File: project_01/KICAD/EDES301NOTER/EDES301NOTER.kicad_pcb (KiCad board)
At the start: 2 copper layers, 61 parts, among them J1 FH12-24S-0.5SH55, Q1 S8050, Q2 BSS84, Q3 BSS84, Q4 BSS84, Q5 BSS138, Q6 BSS84, Q7 BSS138, U1 POCKETBEAGLE, U2 DRV5032FCDBZR, U3 TPS613222ADBVR, U7 PMF250XNEX

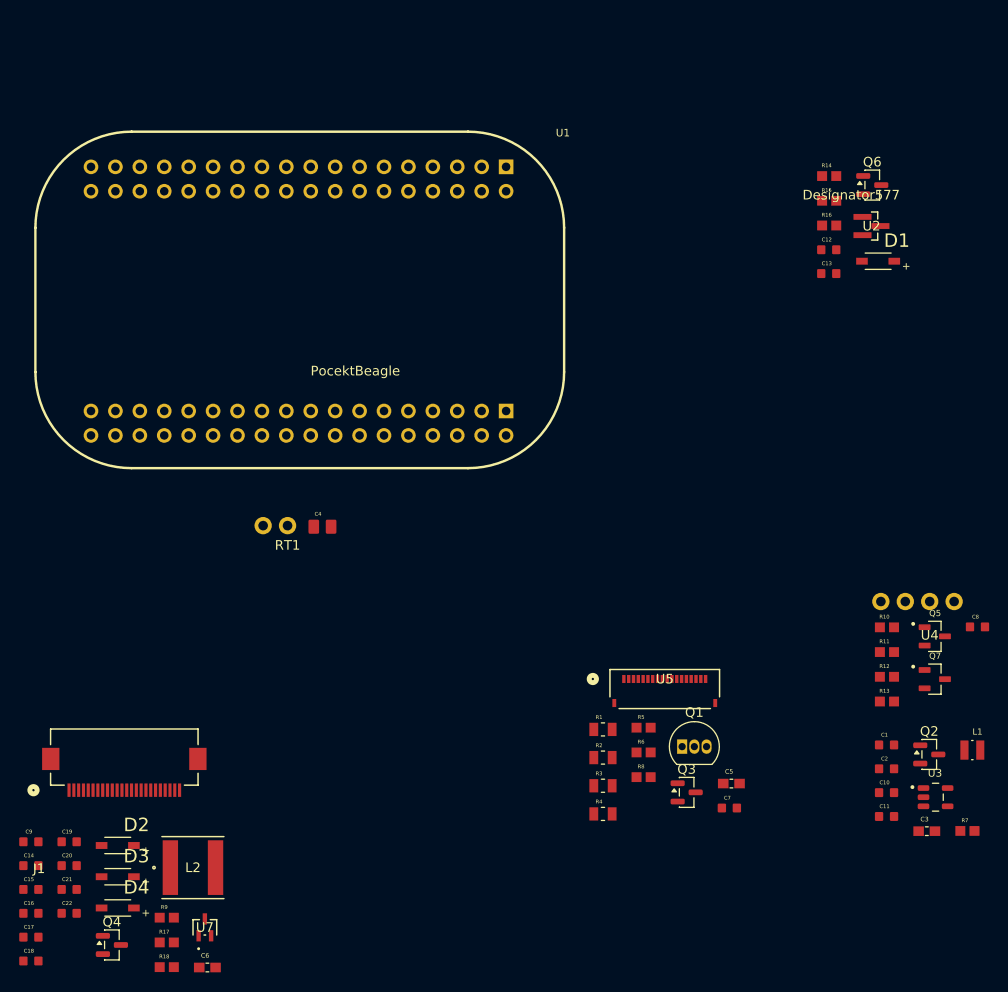
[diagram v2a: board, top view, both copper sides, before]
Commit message: Revise Boost5V schematic and add STIKE symbols
Refactor Boost5V.kicad_sch: updated title block and paper size, reorganized and renamed many symbol definitions (capacitor/inductor/diode/resistor/LED/driver), adjusted pin assignments, footprints, datasheet links and symbol graphics. Added new STIKE-related schematic symbols (Slide Switch, LipoConnection) and multiple KiCad footprint/symbol files under KICAD Files. Added project backup zips and freerouting.dsn, removed a temporary .kicad_sch.lck, and updated project metadata files (.kicad_pcb, .kicad_prl, .kicad_pro, .kicad_sch).
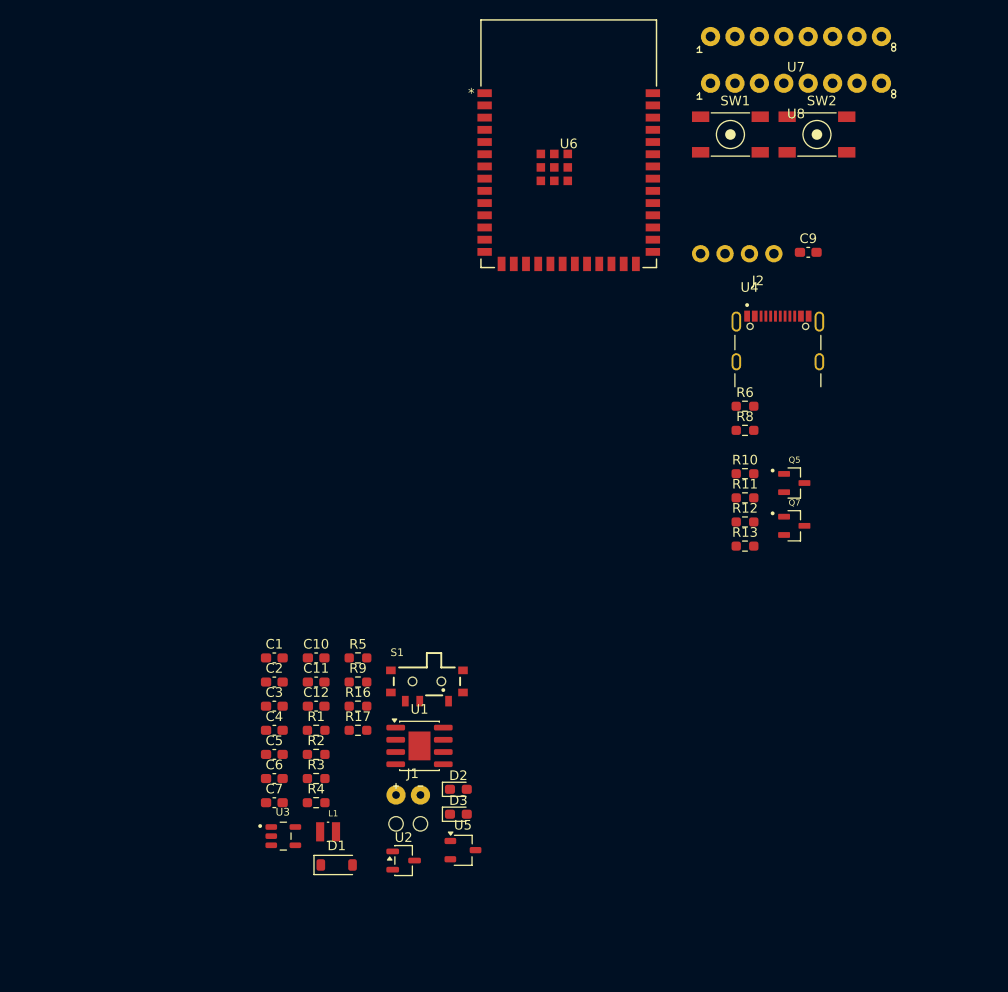
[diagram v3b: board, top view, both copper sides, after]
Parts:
- removed C13, C14, C16, C17, C19, C20, C21, C22, C8: 1uF, Footprints:CAPC1608X90N
- removed C15, C18: 4.7uF, Footprints:CAPC1608X90N
- removed D4: B0530W-7-F, B0530W-7-F:SOD3715X145N
- removed L2: 47uH, IFSC2020DEER470M01:IND_IFSC-2020DE-01_VIS
- removed Q1: S8050, Package_TO_SOT_THT:TO-92_Inline
- removed Q2, Q3, Q4, Q6: BSS84, Package_TO_SOT_SMD:SOT-23
- removed R14: 10k, Footprints:RESC1607X60N
- removed R15, R7: 100k, Footprints:RESC1607X60N
- removed R18: 2.2, Footprints:RESC1607X60N
- removed RT1: NXRT15XH103FA1B040, HomeBrew:2_Wire_Connector
- added J2: UJ20-C-H-G-SMT-1-P16-TR, STIKE:SAMESKY_UJ20-C-H-G-SMT-1-P16-TR, F.Cu at (141.7, 72.0)
- added S1: ~, STIKE:450404015514, F.Cu at (105.2, 102.7)
- added SW1: Boot, STIKE:MembraneButton, F.Cu at (136.8, 56.0)
- added SW2: RST, STIKE:MembraneButton, F.Cu at (145.8, 56.0)
- added U6: ESP32-S3-WROOM-1-N16R8, STIKE:ESP32-S3-WROOM-1_EXP, F.Cu at (120.0, 46.8)
- added U8: ~, STIKE:THROUGH8, F.Cu at (142.3, 40.5)
- C1, C10, C11, C12, C2, C9: footprint Footprints:CAPC1608X90N -> Capacitor_SMD:C_0603_1608Metric_Pad1.08x0.95mm_HandSolder
- C3, C6: value 0.1uF -> 1uF; footprint Footprints:CAPC1608X90 -> Capacitor_SMD:C_0603_1608Metric_Pad1.08x0.95mm_HandSolder
- C4: value 47uF -> 1uF; footprint Footprints:CAPC2012X145N -> Capacitor_SMD:C_0603_1608Metric_Pad1.08x0.95mm_HandSolder
- C5: value 0.1uF -> 4.7uF; footprint Footprints:CAPC1608X90 -> Capacitor_SMD:C_0603_1608Metric_Pad1.08x0.95mm_HandSolder
- C7: value 1uF -> 0.1uF; footprint Footprints:CAPC1608X90N -> Capacitor_SMD:C_0603_1608Metric_Pad1.08x0.95mm_HandSolder
- D1: value B0530W-7-F -> BAT41ZFILM; footprint B0530W-7-F:SOD3715X145N -> Diode_SMD:D_SOD-123
- D2: value B0530W-7-F -> LED_RED; footprint B0530W-7-F:SOD3715X145N -> Diode_SMD:D_0603_1608Metric_Pad1.05x0.95mm_HandSolder
- D3: value B0530W-7-F -> LED_GRN; footprint B0530W-7-F:SOD3715X145N -> Diode_SMD:D_0603_1608Metric_Pad1.05x0.95mm_HandSolder
- J1: value FH12-24S-0.5SH55 -> ~; footprint CF4224FH0R0-05-NH:CONN24X1_FH12-24S-0.5SH55_HIR -> STIKE:LipoConnection
- R1, R2, R3, R4: value 10R -> 1K; footprint Footprints:RESC2012X60N -> Resistor_SMD:R_0603_1608Metric_Pad0.98x0.95mm_HandSolder
- R10, R11, R12, R13, R16, R5: footprint Footprints:RESC1607X60N -> Resistor_SMD:R_0603_1608Metric_Pad0.98x0.95mm_HandSolder
- R17: value 1M -> 1K; footprint Footprints:RESC1607X60N -> Resistor_SMD:R_0603_1608Metric_Pad0.98x0.95mm_HandSolder
- R6: value 1K -> 5.1K; footprint Footprints:RESC1607X60N -> Resistor_SMD:R_0603_1608Metric_Pad0.98x0.95mm_HandSolder
- R8: value 100k -> 5.1K; footprint Footprints:RESC1607X60N -> Resistor_SMD:R_0603_1608Metric_Pad0.98x0.95mm_HandSolder
- R9: value 100k -> 1K; footprint Footprints:RESC1607X60N -> Resistor_SMD:R_0603_1608Metric_Pad0.98x0.95mm_HandSolder
- U1: value POCKETBEAGLE -> TPB4056A20-ES1R; footprint POCKETBEAGLE (1):POCKETBEAGLE -> STIKE:TPB4056A20-ES1R
- U2: value DRV5032FCDBZR -> DRV5032FADBZR; footprint DRV5032FCDBZR:DBZ0003A-IPC_A -> Package_TO_SOT_SMD:SOT-23-3
- U5: value ~ -> XC6206P332MR-G; footprint FH34SRJ-18S-0.5SH:CONN18x1_FH34SRJ-18S-0.5SH50_HIR -> Package_TO_SOT_SMD:TSOT-23
- U7: value PMF250XNEX -> ~; footprint PMF250XNEX:PMF250XNEX_NEX -> STIKE:THROUGH8
- moved U7 110.5 mm to (142.3, 35.6)
- moved C9 101.5 mm to (144.9, 58.0)
- moved D1 84.4 mm to (95.8, 121.8)
- moved U2 82.0 mm to (102.8, 121.3)
- moved C12 71.4 mm to (93.7, 105.3)
- moved R16 70.0 mm to (98.1, 105.3)
- moved C3 69.1 mm to (89.4, 105.3)
- moved U3 68.0 mm to (90.3, 118.8)
- moved L1 67.6 mm to (94.9, 118.3)
- moved U1 65.5 mm to (104.5, 109.4), turned to 0 degrees
- moved C1 64.3 mm to (89.4, 100.2)
- moved C2 64.3 mm to (89.4, 102.8)
- moved C10 61.0 mm to (93.7, 100.2)
- moved C11 61.0 mm to (93.7, 102.8)
- moved C5 47.6 mm to (89.4, 110.3)
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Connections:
- net /CardKB/CARD_SCL renamed /ESP32-S3-N16R8/KEY_SDA
- net /CardKB/CARD_SDA renamed /ESP32-S3-N16R8/KEY_SCL
- C1 pad 1: Net-(Q2-D) -> /Power Circuitry/BAT+
- C1 pad 2: -BATT -> GND
- C10 pad 2: -BATT -> GND
- C11 pad 2: -BATT -> GND
- C12 pad 1: +3.3V -> /Power Circuitry/ 
- C12 pad 2: -BATT -> /ESP32-S3-N16R8/WAKE_BTN
- C2 pad 2: -BATT -> GND
- C3 pad 1: Net-(Q2-D) -> +5V
- C3 pad 2: -BATT -> GND
- C4 pad 1: -BATT -> /Power Circuitry/BAT+
- C4 pad 2: +3.3V -> GND
- C5 pad 1: Net-(Q3-D) -> GND
- C5 pad 2: -BATT -> +5VA
- C6 pad 1: /ePaper Support Circuit/VCI -> +3.3V
- C6 pad 2: -BATT -> unconnected-(C6-Pad2)
- C7 pad 1: -BATT -> +3.3V
- C7 pad 2: Net-(Q3-D) -> GND
- C9 pad 1: /ePaper Support Circuit/PREVGH -> +5V
- C9 pad 2: -BATT -> GND
- J1 pad 1: unconnected-(J1-Pad1) -> Net-(J1-Batt_Pos)
- J1 pad 2: /ePaper Support Circuit/GDR -> GND
- L1 pad 1: Net-(Q2-D) -> /Power Circuitry/BAT+
- Q5 pad 3: /CardKB/DATA -> /LogicLevelConverter/HV1
- Q7 pad 3: /CardKB/DATA -> /LogicLevelConverter/HV2
- R1 pad 1: Net-(Q1-C) -> GND
- R1 pad 2: Net-(U5-LEDK1) -> Net-(R1-Pad2)
- R11 pad 2: /CardKB/DATA -> /LogicLevelConverter/HV1
- R13 pad 2: /CardKB/DATA -> /LogicLevelConverter/HV2
- R16 pad 1: -BATT -> /ESP32-S3-N16R8/WAKE_BTN
- R16 pad 2: Net-(R15-Pad2) -> GND
- R17 pad 1: /ePaper Support Circuit/GDR -> Net-(D3-A)
- R17 pad 2: -BATT -> +5VA
- R2 pad 1: Net-(Q1-C) -> Net-(U1-IMIN)
- R2 pad 2: Net-(U5-LEDK2) -> Net-(R2-Pad2)
- R3 pad 1: Net-(Q1-C) -> Net-(R2-Pad2)
- R3 pad 2: Net-(U5-LEDK3) -> GND
- R4 pad 1: Net-(Q1-C) -> GND
- R4 pad 2: Net-(U5-LEDK4) -> Net-(R1-Pad2)
- R5 pad 1: Net-(Q1-B) -> Net-(U1-IREF)
- R5 pad 2: /TFT Display/TFT_BL -> Net-(R1-Pad2)
- R6 pad 1: Net-(Q1-B) -> Net-(J2-CC1)
- R6 pad 2: -BATT -> GND
- R8 pad 1: /TFT Display/TFT_BL -> Net-(J2-CC2)
- R8 pad 2: +3.3V -> GND
- R9 pad 1: /ePaper Support Circuit/EPPR_PWR -> Net-(D2-A)
- R9 pad 2: +3.3V -> +5VA
- U1 pad 1: unconnected-(U1-VIN-Pad1) -> +5VA
- U1 pad 2: /TFT_D/C -> Net-(D3-K)
- U1 pad 3: unconnected-(U1-USB1.DRVVBUS-Pad3) -> Net-(D2-K)
- U1 pad 4: unconnected-(U1-GPIO89-Pad4) -> +5VA
- U1 pad 5: unconnected-(U1-USB1.VBUS-Pad5) -> GND
- U1 pad 6: /TFT_CSX -> Net-(U1-IMIN)
- U1 pad 7: unconnected-(U1-USB1.VIN-Pad7) -> Net-(U1-IREF)
- U1 pad 8: /TFT_SDL -> /Power Circuitry/BAT+
- U2 pad 2: /Hall Effect Power Switch/PB_LID -> /Power Circuitry/ 
- U2 pad 3: -BATT -> GND
- U3 pad 2: -BATT -> GND
- U4 pad 1: +5V -> GND
- U4 pad 2: /CardKB/DATA -> +5V
- U4 pad 3: /CardKB/DATA -> /LogicLevelConverter/HV1
- U4 pad 4: -BATT -> /LogicLevelConverter/HV2
- U5 pad 1: -BATT -> GND
- U5 pad 2: /TFT Display/TFT_RST -> +3.3V
- U5 pad 3: /TFT Display/TFT_SDL -> +5V
- U7 pad 1: /ePaper Support Circuit/GDR -> /ESP32-S3-N16R8/EP_BUSY
- U7 pad 2: /ePaper Support Circuit/RESE -> /ESP32-S3-N16R8/EP_RST
- U7 pad 3: Net-(U7-D) -> /ESP32-S3-N16R8/EP_DC
